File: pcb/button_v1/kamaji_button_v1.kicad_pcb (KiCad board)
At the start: 2 copper layers, 30 x 37 mm, 7 parts, among them J1 RJ10, SW2 SW_Push_LED

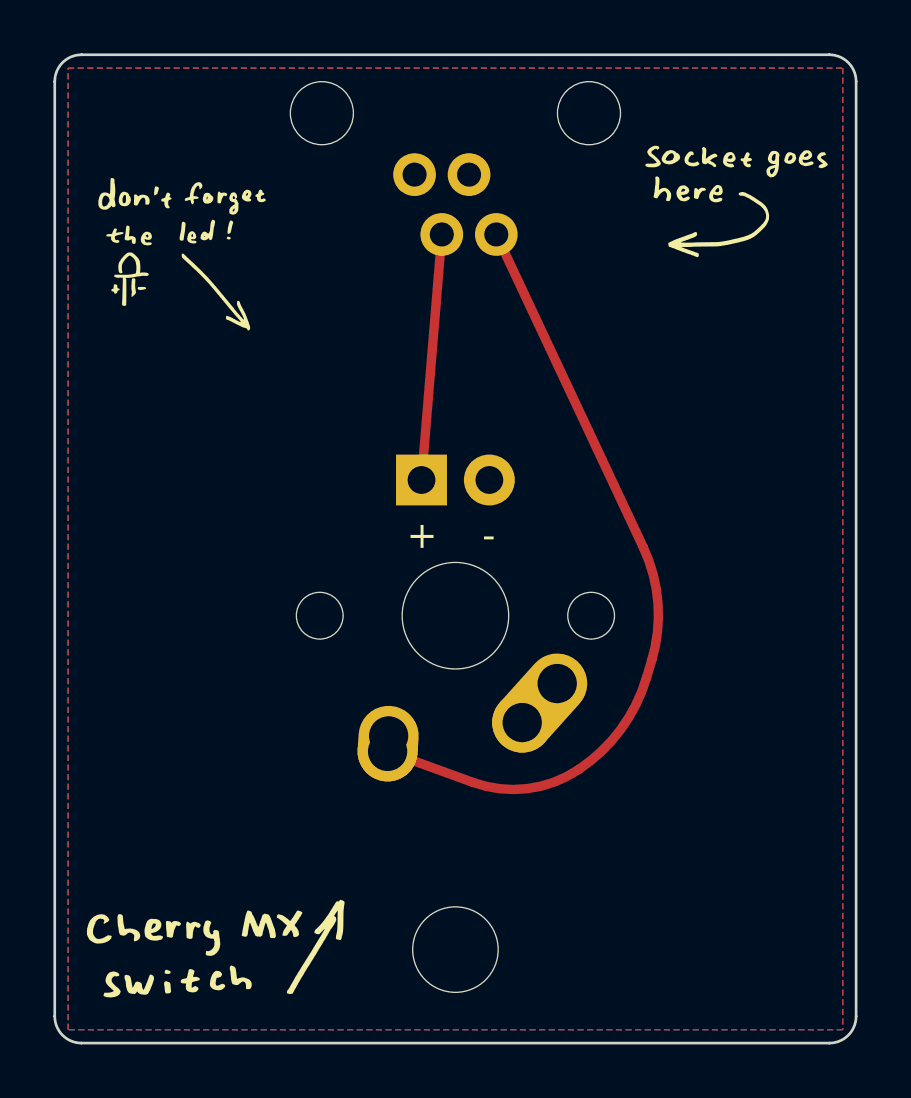
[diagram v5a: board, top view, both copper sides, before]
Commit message: button pcb: replace the switch footprint
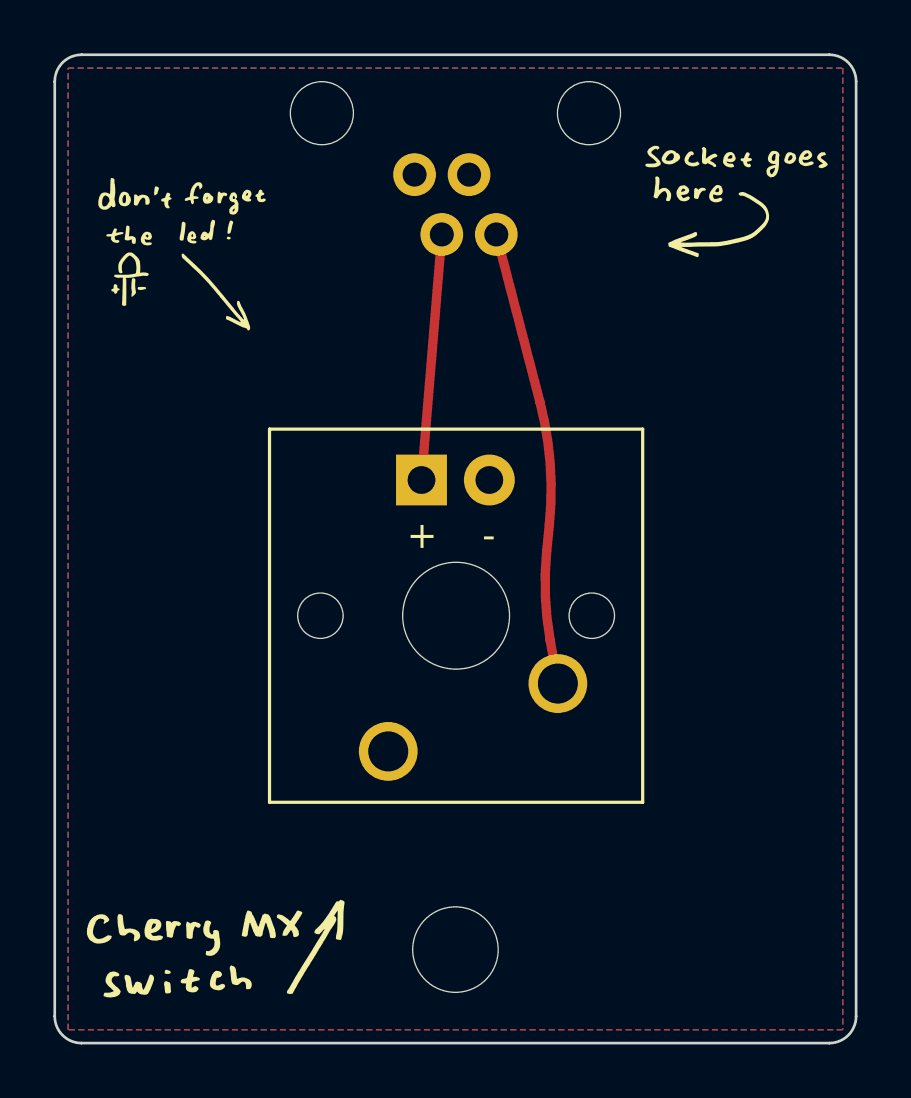
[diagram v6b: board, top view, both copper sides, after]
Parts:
- SW2: footprint mx_alps_hybrid:MX-1U -> kamaji:SW_Cherry_MX_1.00u_PCB
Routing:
- net Net-(J1-Pad4): track 29.8 -> 17.1 mm
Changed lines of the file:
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@@
       ) (layer "F.SilkS") (width 0) (fill solid))
   )
-  (footprint "mx_alps_hybrid:MX-1U" (layer "F.Cu")
+  (footprint "kamaji:SW_Cherry_MX_1.00u_PCB" (layer "F.Cu")
     (at 65 71 180)
-    (property "Sheetfile" "File: kamaji_button_v1.kicad_sch")
+    (descr "Cherry MX keyswitch, 1.00u, PCB mount, http://cherryamericas.com/wp-content/uploads/2014/12/mx_cat.pdf")
+    (tags "Cherry MX keyswitch 1.00u PCB")
+    (property "Sheetfile" "kamaji_button_v1.kicad_sch")
     (property "Sheetname" "")
     (attr through_hole)
-    (fp_text reference "SW2" (at 0 3.175) (layer "Dwgs.User") hide
+    (fp_text reference "SW2" (at -0.025 -7.874 180) (layer "F.SilkS") hide
       (effects (font (size 1 1) (thickness 0.15)))
     )
-    (fp_text value "SW_Push_LED" (at 0 -7.9375) (layer "Dwgs.User") hide
+    (fp_text value "SW_Push_LED" (at -0.025 7.874 180) (layer "F.Fab")
       (effects (font (size 1 1) (thickness 0.15)))
     )
-    (fp_line (start 5 7) (end 7 7) (layer "Dwgs.User") (width 0.15))
-    (fp_line (start -9.525 9.525) (end -9.525 -9.525) (layer "Dwgs.User") (width 0.15))
-    (fp_line (start 5 -7) (end 7 -7) (layer "Dwgs.User") (width 0.15))
-    (fp_line (start -7 5) (end -7 7) (layer "Dwgs.User") (width 0.15))
-    (fp_line (start 9.525 -9.525) (end 9.525 9.525) (layer "Dwgs.User") (width 0.15))
-    (fp_line (start -7 -7) (end -7 -5) (layer "Dwgs.User") (width 0.15))
-    (fp_line (start 9.525 9.525) (end -9.525 9.525) (layer "Dwgs.User") (width 0.15))
-    (fp_line (start -7 7) (end -5 7) (layer "Dwgs.User") (width 0.15))
-    (fp_line (start 7 7) (end 7 5) (layer "Dwgs.User") (width 0.15))
-    (fp_line (start -5 -7) (end -7 -7) (layer "Dwgs.User") (width 0.15))
-    (fp_line (start -9.525 -9.525) (end 9.525 -9.525) (layer "Dwgs.User") (width 0.15))
-    (fp_line (start 7 -7) (end 7 -5) (layer "Dwgs.User") (width 0.15))
-    (pad "" np_thru_hole circle locked (at -5.08 0 228.0996) (size 1.75 1.75) (drill 1.75) (layers *.Cu *.Mask))
-    (pad "" np_thru_hole circle locked (at 5.08 0 228.0996) (size 1.75 1.75) (drill 1.75) (layers *.Cu *.Mask))
-    (pad "" np_thru_hole circle locked (at 0 0 180) (size 3.9878 3.9878) (drill 3.9878) (layers *.Cu *.Mask))
-    (pad "1" thru_hole oval locked (at -3.81 -2.54 228.0996) (size 4.211556 2.25) (drill 1.47 (offset 0.980778 0)) (layers *.Cu "B.Mask")
-      (net 1 "GND") (pinfunction "1") (pintype "passive"))
-    (pad "1" thru_hole circle locked (at -2.5 -4 180) (size 2.25 2.25) (drill 1.47) (layers *.Cu "B.Mask")
+    (fp_text user "${REFERENCE}" (at -0.025 -7.874 180) (layer "F.Fab")
+      (effects (font (size 1 1) (thickness 0.15)))
+    )
+    (fp_line (start -7.01 6.985) (end -7.01 -6.985) (layer "F.SilkS") (width 0.12))
+    (fp_line (start -7.01 -6.985) (end 6.96 -6.985) (layer "F.SilkS") (width 0.12))
+    (fp_line (start 6.96 6.985) (end -7.01 6.985) (layer "F.SilkS") (width 0.12))
+    (fp_line (start 6.96 -6.985) (end 6.96 6.985) (layer "F.SilkS") (width 0.12))
+    (fp_line (start 9.5 -9.525) (end 9.5 9.525) (layer "Dwgs.User") (width 0.15))
+    (fp_line (start -9.55 -9.525) (end 9.5 -9.525) (layer "Dwgs.User") (width 0.15))
+    (fp_line (start -9.55 9.525) (end -9.55 -9.525) (layer "Dwgs.User") (width 0.15))
+    (fp_line (start 9.5 9.525) (end -9.55 9.525) (layer "Dwgs.User") (width 0.15))
+    (fp_line (start 6.575 -6.6) (end 6.575 6.6) (layer "F.CrtYd") (width 0.05))
+    (fp_line (start -6.625 6.6) (end -6.625 -6.6) (layer "F.CrtYd") (width 0.05))
+    (fp_line (start -6.625 -6.6) (end 6.575 -6.6) (layer "F.CrtYd") (width 0.05))
+    (fp_line (start 6.575 6.6) (end -6.625 6.6) (layer "F.CrtYd") (width 0.05))
+    (fp_line (start 6.325 6.35) (end -6.375 6.35) (layer "F.Fab") (width 0.1))
+    (fp_line (start 6.325 -6.35) (end 6.325 6.35) (layer "F.Fab") (width 0.1))
+    (fp_line (start -6.375 -6.35) (end 6.325 -6.35) (layer "F.Fab") (width 0.1))
+    (fp_line (start -6.375 6.35) (end -6.375 -6.35) (layer "F.Fab") (width 0.1))
+    (pad "" np_thru_hole circle (at 5.055 0 180) (size 1.7 1.7) (drill 1.7) (layers *.Cu *.Mask))
+    (pad "" np_thru_hole circle (at -5.105 0 180) (size 1.7 1.7) (drill 1.7) (layers *.Cu *.Mask))
+    (pad "" np_thru_hole circle (at -0.025 0 180) (size 4 4) (drill 4) (layers *.Cu *.Mask))
+    (pad "1" thru_hole circle (at 2.515 -5.08 180) (size 2.2 2.2) (drill 1.5) (layers *.Cu *.Mask)
       (net 1 "GND") (pinfunction "1") (pintype "passive"))
-    (pad "2" thru_hole circle locked (at 2.54 -5.08 180) (size 2.25 2.25) (drill 1.47) (layers *.Cu "B.Mask")
-      (net 2 "Net-(J1-Pad4)") (pinfunction "2") (pintype "passive"))
-    (pad "2" thru_hole oval locked (at 2.5 -4.5 266.0548) (size 2.831378 2.25) (drill 1.47 (offset 0.290689 0)) (layers *.Cu "B.Mask")
+    (pad "2" thru_hole circle (at -3.835 -2.54 180) (size 2.2 2.2) (drill 1.5) (layers *.Cu *.Mask)
       (net 2 "Net-(J1-Pad4)") (pinfunction "2") (pintype "passive"))
-    (pad "3" thru_hole circle locked (at -1.27 5.08 180) (size 1.905 1.905) (drill 1.04) (layers *.Cu "B.Mask")
+    (pad "3" thru_hole circle (at -1.27 5.08 180) (size 1.905 1.905) (drill 1.04) (layers *.Cu *.Mask)
       (net 1 "GND") (pinfunction "K") (pintype "passive"))
-    (pad "4" thru_hole rect locked (at 1.27 5.08 180) (size 1.905 1.905) (drill 1.04) (layers *.Cu "B.Mask")
+    (pad "4" thru_hole rect (at 1.27 5.08 180) (size 1.905 1.905) (drill 1.04) (layers *.Cu *.Mask)
       (net 3 "Net-(J1-Pad2)") (pinfunction "A") (pintype "passive"))
-    (model "/Users/ilya/projects/kamaji/pcb/lib/keyswitch-kicad-library/library/3dmodels/3d-library.3dshapes/SW_Cherry_MX_PCB.wrl"
+    (model "${KICAD6_3DMODEL_DIR}/Button_Switch_Keyboard.3dshapes/SW_Cherry_MX_1.00u_PCB.wrl"
       (offset (xyz 0 0 0))
       (scale (xyz 1 1 1))
@@
   (footprint "kamaji:RJ10" (layer "F.Cu")
     (at 65 46.1875 180)
-    (property "Sheetfile" "File: kamaji_button_v1.kicad_sch")
+    (property "Sheetfile" "kamaji_button_v1.kicad_sch")
     (property "Sheetname" "")
     (attr through_hole)
@@
     (style (thickness 0.2) (arrow_length 1.27) (text_position_mode 0) (extension_height 0.58642) (extension_offset 0.5) keep_text_aligned)
   )
-  (segment (start 72.036578 68.449191) (end 66.53 56.7275) (width 0.35) (layer "F.Cu") (net 2))
-  (segment (start 65.665902 77.243578) (end 62.46 76.08) (width 0.35) (layer "F.Cu") (net 2))
-  (segment (start 69.624999 76.749999) (end 69.594758 76.770161) (width 0.35) (layer "F.Cu") (net 2))
-  (segment (start 72.348917 72.670273) (end 72.147529 73.341567) (width 0.35) (layer "F.Cu") (net 2))
-  (arc (start 72.036578 68.449191) (mid 72.582601 70.530885) (end 72.348917 72.670273) (width 0.35) (layer "F.Cu") (net 2))
-  (arc (start 72.147529 73.341567) (mid 71.183779 75.265969) (end 69.624999 76.749999) (width 0.35) (layer "F.Cu") (net 2))
-  (arc (start 65.665902 77.243578) (mid 67.686764 77.47521) (end 69.594758 76.770161) (width 0.35) (layer "F.Cu") (net 2))
-  (segment (start 64.49 56.7275) (end 63.73 65.92) (width 0.35) (layer "F.Cu") (net 3))
+  (segment (start 68.163978 63.000283) (end 66.53 56.7275) (width 0.35) (layer "F.Cu") (net 2))
+  (segment (start 68.5425 71.895) (end 68.835 73.54) (width 0.35) (layer "F.Cu") (net 2))
+  (segment (start 68.41625 68.587489) (end 68.518674 67.563251) (width 0.35) (layer "F.Cu") (net 2))
+  (arc (start 68.163978 63.000283) (mid 68.544049 65.266008) (end 68.518674 67.563251) (width 0.35) (layer "F.Cu") (net 2))
+  (arc (start 68.41625 68.587489) (mid 68.365233 70.245601) (end 68.5425 71.895) (width 0.35) (layer "F.Cu") (net 2))
+  (segment (start 63.73 65.92) (end 64.49 56.7275) (width 0.35) (layer "F.Cu") (net 3))
   (zone (net 1) (net_name "GND") (layers F&B.Cu) (hatch edge 0.508)
     (connect_pads (clearance 0.508))

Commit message: button pcb: update silkscreen
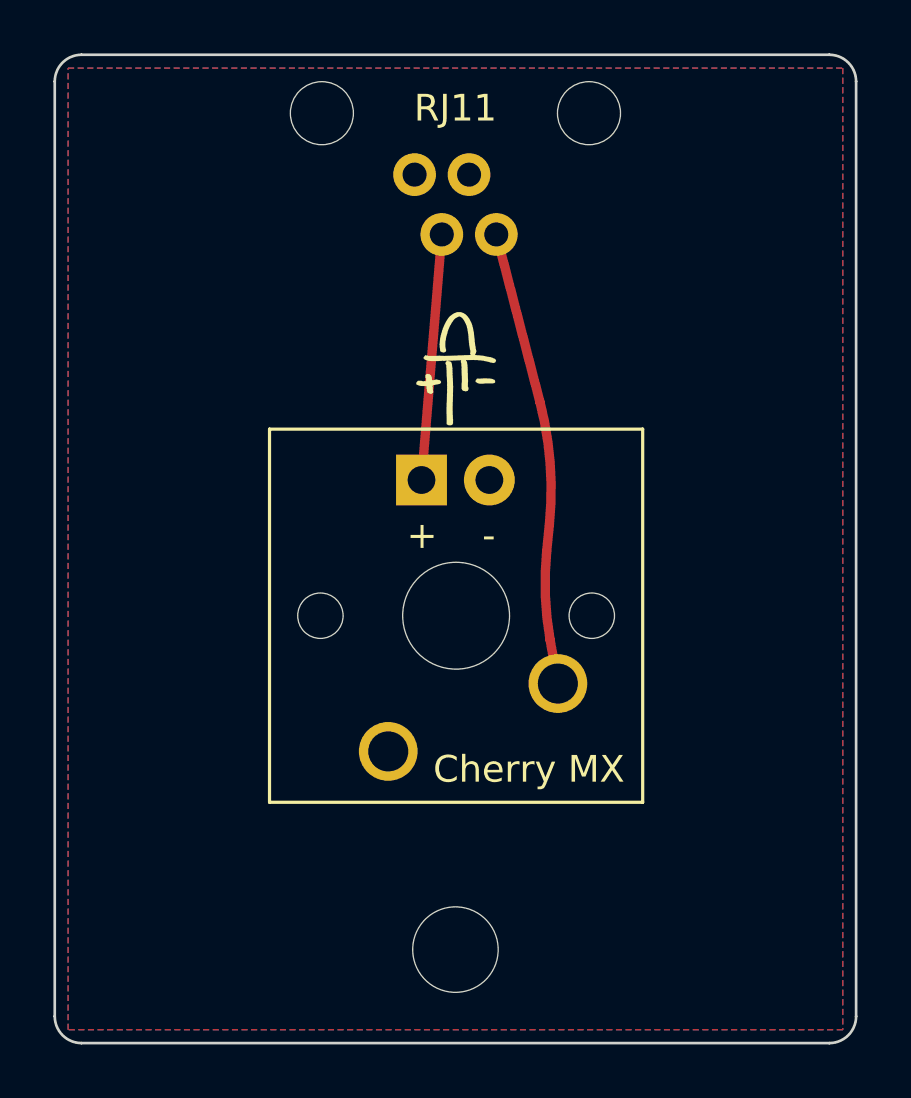
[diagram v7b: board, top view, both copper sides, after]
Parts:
- removed the G*** at (56.0, 83.5)
- removed the G*** at (54.8, 57.5)
- removed the G*** at (75.5, 55.5)
- removed the G*** at (75.5, 68.5)
- added G***: LOGO, LOGO, F.Cu at (65.0, 61.8)
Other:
- board text added: "Cherry MX"
- board text added: "Kamaji Button v1.2"
- board text added: "RJ11"
- board text added: "github.com/iley/kamaji"
- board text removed: "v1.1 12/2022"

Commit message: Minor tweaks to button PCB silkscreen
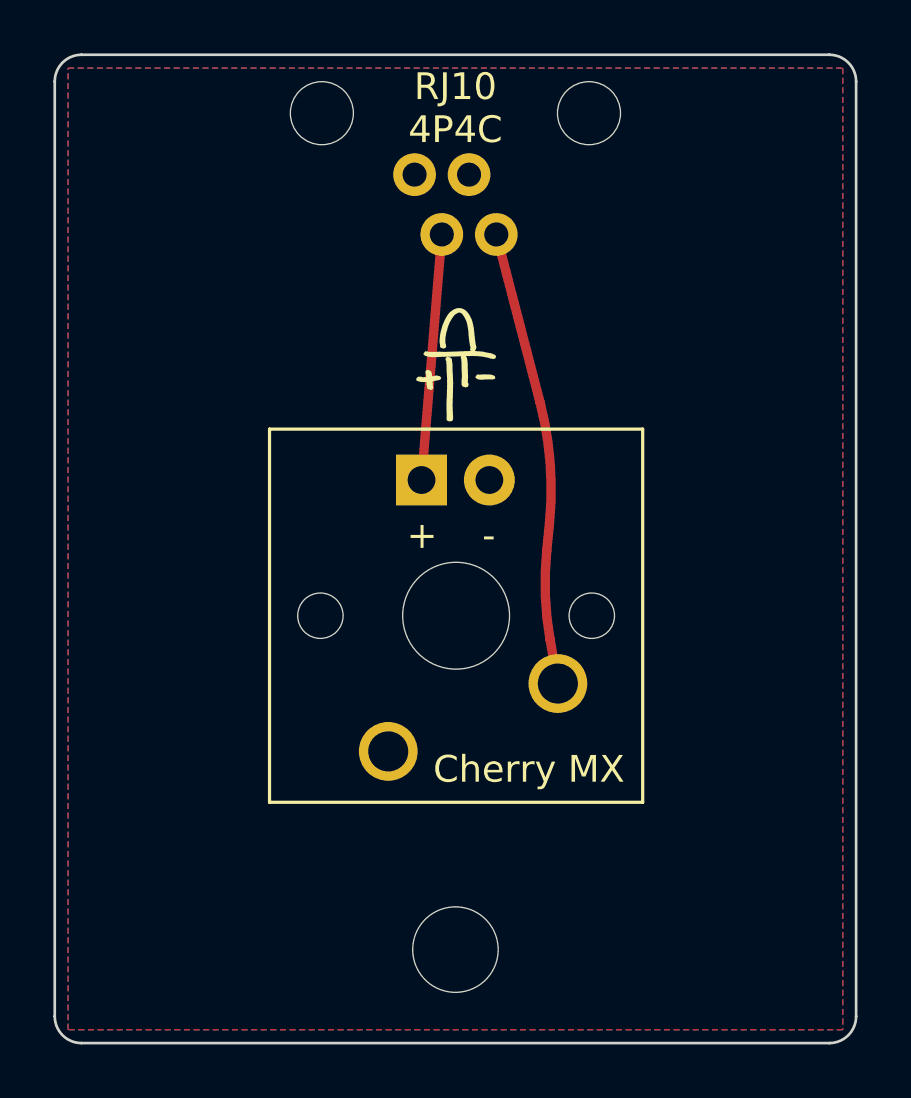
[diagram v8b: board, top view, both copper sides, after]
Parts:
- moved G*** 0.15 mm to (65.0, 61.6)
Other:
- board text added: "Kamaji Button v1.3"
- board text added: "RJ10 4P4C"
- board text removed: "Kamaji Button v1.2"
- board text removed: "RJ11"
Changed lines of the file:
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@@
   )
   (footprint "LOGO" (layer "F.Cu")
-    (at 65.025 61.75)
+    (at 65.025 61.6)
     (attr board_only exclude_from_pos_files exclude_from_bom)
     (fp_text reference "G***" (at 0 0) (layer "F.SilkS") hide
@@
     (effects (font (size 1.6 1.6) (thickness 0.2)) (justify mirror))
   )
-  (gr_text "Kamaji Button v1.2" (at 75.5 68 270) (layer "B.SilkS")
+  (gr_text "Kamaji Button v1.3" (at 75.5 68 270) (layer "B.SilkS")
     (effects (font (size 1.6 1.6) (thickness 0.2)) (justify mirror))
   )
@@
     (effects (font (size 1 1) (thickness 0.15)))
   )
-  (gr_text "RJ11" (at 65 52) (layer "F.SilkS")
+  (gr_text "RJ10\n4P4C" (at 65 52) (layer "F.SilkS")
     (effects (font (size 1 1) (thickness 0.15)))
   )
